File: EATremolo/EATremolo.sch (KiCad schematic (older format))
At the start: 37 parts, among them J1 JACK__MONO_2P_NC, J2 BARREL_JACK, J3 JACK__MONO_2P_NC, Q1 Q_NJFET_DSG, Q2 Q_NPN_EBC, Q3 Q_NPN_EBC, Q4 Q_NJFET_DSG, SW1 SW_3PDT_on_on

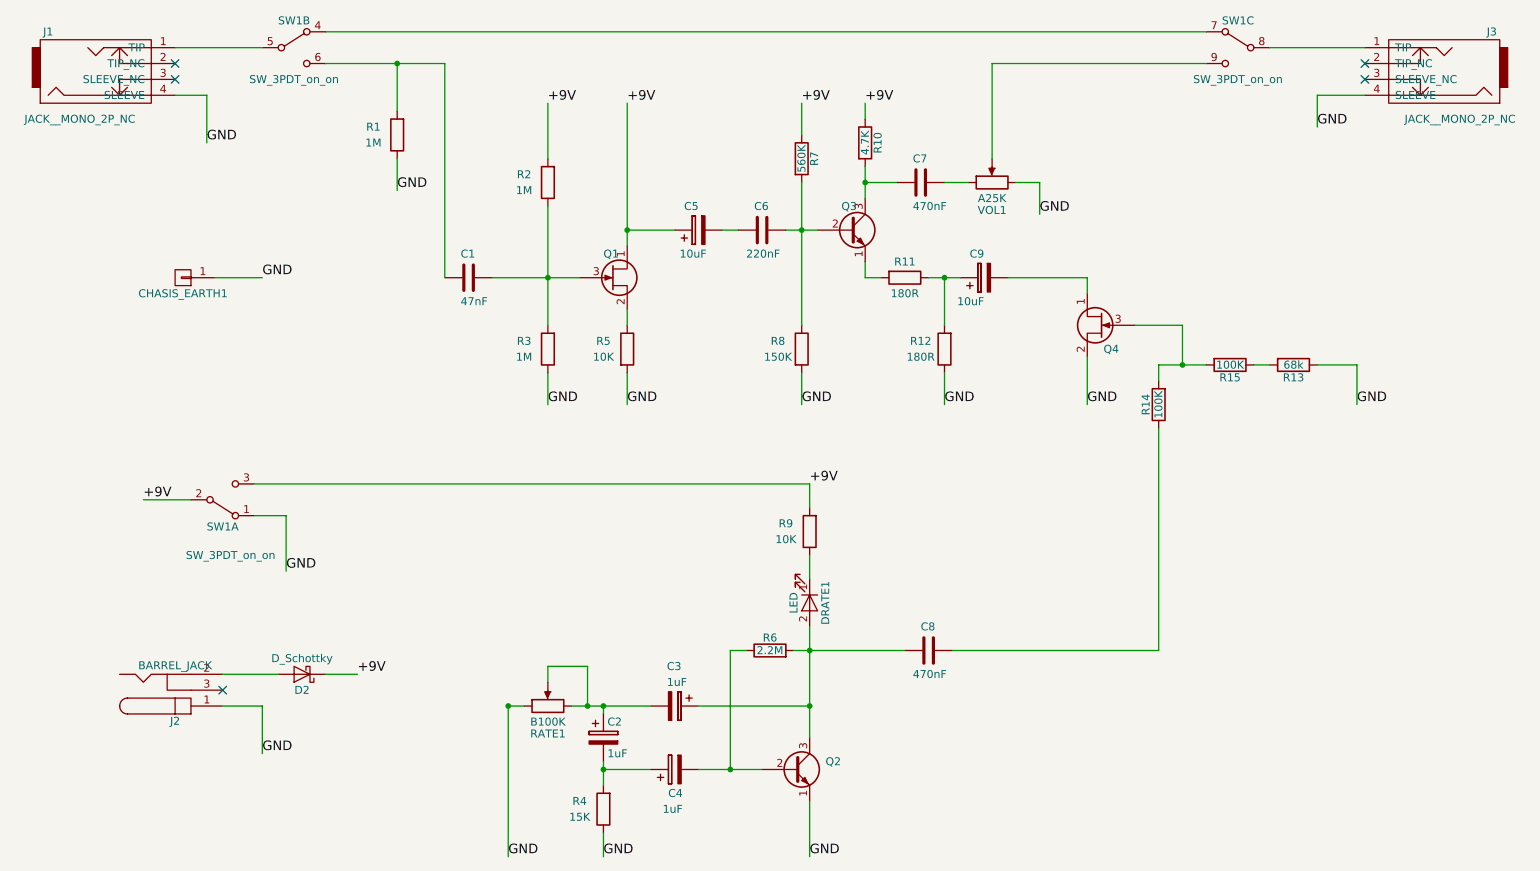
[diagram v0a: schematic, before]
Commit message: EA Tremolo Layout completed
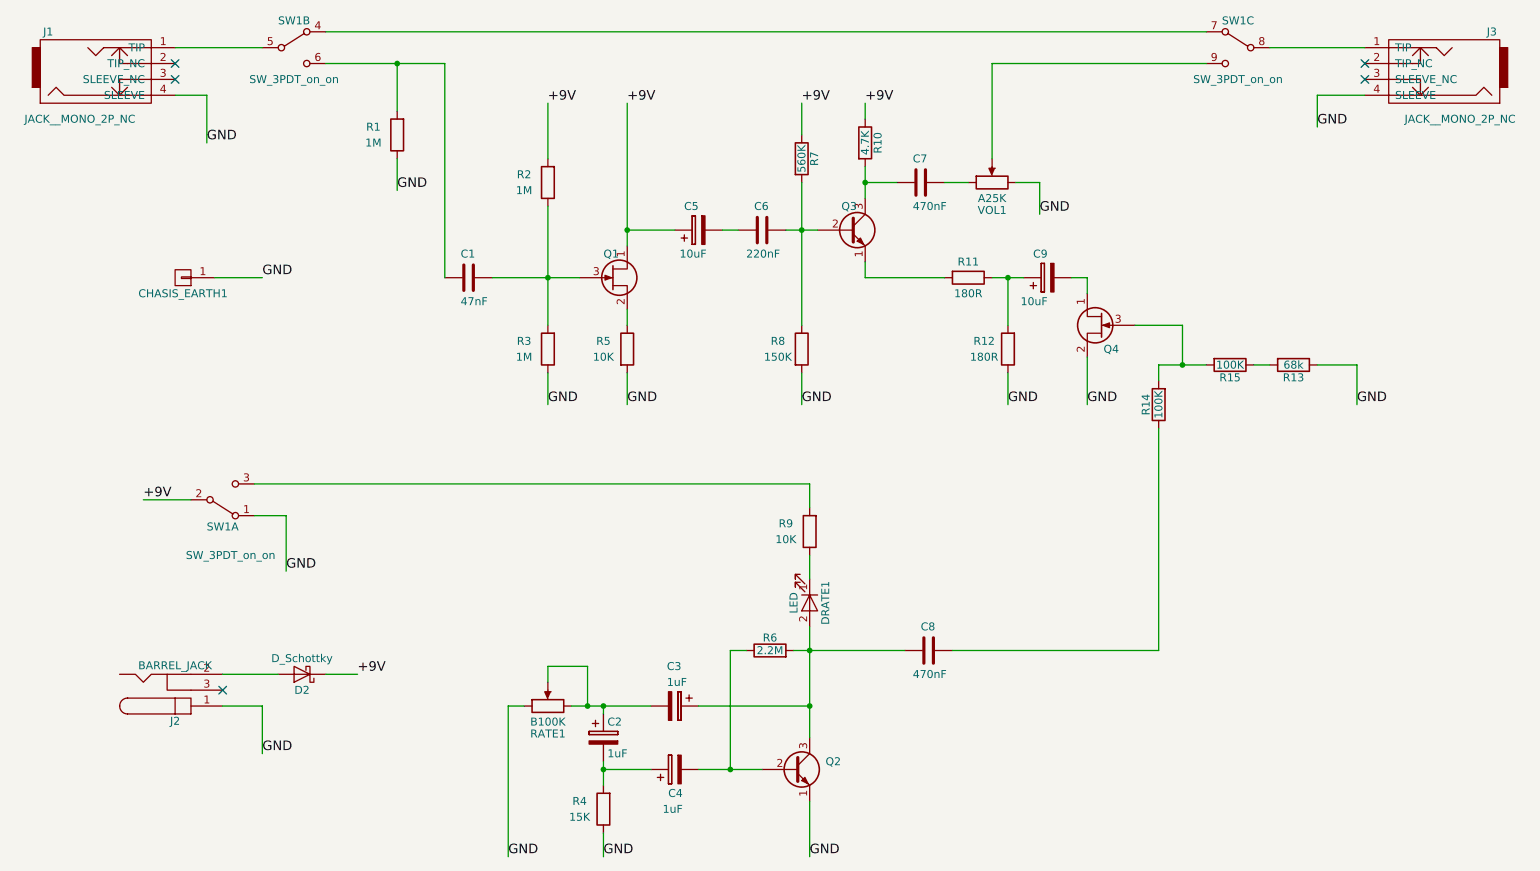
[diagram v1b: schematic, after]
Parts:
- D2: footprint Diodes_THT:D_DO-41_SOD81_P10.16mm_Horizontal -> Diodes_THT:D_DO-41_SOD81_P2.54mm_Vertical_AnodeUp
- R1, R10, R12, R13, R14, R15, R2, R3, R4, R5, R6, R7, R8, R9: footprint R_Axial_DIN0207_L6.3mm_D2.5mm_P7:R_Axial_DIN0207_L6.3mm_D2.5mm_P7.62mm_Horizontal_PS2_DH1 -> R_Axial_DIN0207_Vertical_2mmPad:R_Axial_DIN0207_Vertical_2mmPad
- R11: footprint R_Axial_DIN0207_L6.3mm_D2.5mm_P7:R_Axial_DIN0207_L6.3mm_D2.5mm_P7.62mm_Horizontal_PS2_DH1 -> Resistors_THT:R_Axial_DIN0207_L6.3mm_D2.5mm_P5.08mm_Vertical
- RATE1, VOL1: footprint TEConnPotentiometer:TEConnPot_23mm_20mm -> Potentiometers:Potentiometer_Omeg_PC16PU_Horizontal
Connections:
- net +9V: no longer R9.2, SW1.3 (C)
- new net: R9.2, SW1.3 (C)
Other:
- moved on the sheet: C9, R11, R12

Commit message: saved EATremolo
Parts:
- C5: footprint CP_Radial_D4_P2_PadSize2_Drill1:CP_Radial_D4_P2_PadSize2_Drill1 -> C_Disc_P5:C_Disc_P5.0mm_2mmPads
- C7: footprint C_Disc_2mmPads:C_Disc_2mmPads -> C_Disc_P5:C_Disc_P5.0mm_2mmPads
- R5: footprint R_Axial_DIN0207_Vertical_2mmPad:R_Axial_DIN0207_Vertical_2mmPad -> R_Axial_DIN0207_P5:R_Axial_DIN0207_P5.08mm_2mmPads
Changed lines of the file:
@@
 F 0 "R5" H 4550 3500 50  0000 C CNN
 F 1 "10K" H 4550 3400 50  0000 C CNN
-F 2 "R_Axial_DIN0207_Vertical_2mmPad:R_Axial_DIN0207_Vertical_2mmPad" V 4630 3450 50  0001 C CNN
+F 2 "R_Axial_DIN0207_P5:R_Axial_DIN0207_P5.08mm_2mmPads" V 4630 3450 50  0001 C CNN
 F 3 "" H 4700 3450 50  0001 C CNN
 	1    4700 3450
@@
 F 0 "C5" V 5300 2700 50  0000 L CNN
 F 1 "10uF" V 5000 2650 50  0000 L CNN
-F 2 "CP_Radial_D4_P2_PadSize2_Drill1:CP_Radial_D4_P2_PadSize2_Drill1" H 5188 2550 50  0001 C CNN
+F 2 "C_Disc_P5:C_Disc_P5.0mm_2mmPads" H 5188 2550 50  0001 C CNN
 F 3 "" H 5150 2700 50  0001 C CNN
 	1    5150 2700
@@
 F 0 "C7" V 6400 2350 50  0000 L CNN
 F 1 "470nF" V 6700 2350 50  0000 L CNN
-F 2 "C_Disc_2mmPads:C_Disc_2mmPads" H 6588 2250 50  0001 C CNN
+F 2 "C_Disc_P5:C_Disc_P5.0mm_2mmPads" H 6588 2250 50  0001 C CNN
 F 3 "" H 6550 2400 50  0001 C CNN
 	1    6550 2400
@@
 	2400 5700 2400 6000
 Wire Wire Line
-	2800 1650 3250 1650
-Wire Wire Line
-	3250 1650 3550 1650
+	2800 1650 3550 1650
 Wire Wire Line
 	3250 1650 3250 1950
@@
 	3250 2250 3250 2450
 Wire Wire Line
-	4200 2550 4200 3000
-Wire Wire Line
-	4200 3000 4200 3300
+	4200 2550 4200 3300
 Wire Wire Line
 	4200 3600 4200 3800
 Connection ~ 3250 1650
 Wire Wire Line
-	3850 3000 4200 3000
-Wire Wire Line
-	4200 3000 4400 3000
+	3850 3000 4400 3000
 Connection ~ 4200 3000
 Wire Wire Line
@@
 	4700 3600 4700 3800
 Wire Wire Line
-	4700 1900 4700 2700
-Wire Wire Line
-	4700 2700 4700 2800
+	4700 1900 4700 2800
 Wire Wire Line
 	5000 2700 4700 2700
@@
 	5800 2100 5800 1900
 Wire Wire Line
-	6200 2300 6200 2400
-Wire Wire Line
-	6200 2400 6200 2500
+	6200 2300 6200 2500
 Connection ~ 5800 2700
 Wire Wire Line
-	5800 2400 5800 2700
-Wire Wire Line
-	5800 2700 5800 3300
-Wire Wire Line
-	5700 2700 5800 2700
-Wire Wire Line
-	5800 2700 5900 2700
+	5800 2400 5800 3300
+Wire Wire Line
+	5700 2700 5900 2700
 Wire Wire Line
 	6200 2900 6200 3000
@@
 	7100 3300 7100 3000
 Wire Wire Line
-	7000 3000 7100 3000
-Wire Wire Line
-	7100 3000 7200 3000
+	7000 3000 7200 3000
 Wire Wire Line
 	7100 3600 7100 3800
@@
 	8050 5350 6750 5350
 Wire Wire Line
-	5850 5200 5850 5350
-Wire Wire Line
-	5850 5350 5850 5700
-Wire Wire Line
-	5850 5700 5850 5900
+	5850 5200 5850 5900
 Connection ~ 5850 5350
 Wire Wire Line
@@
 	5850 6300 5850 6650
 Wire Wire Line
-	5750 5350 5850 5350
-Wire Wire Line
-	5850 5350 6450 5350
+	5750 5350 6450 5350
 Wire Wire Line
 	5150 5700 5850 5700
 Connection ~ 5850 5700
 Wire Wire Line
-	4350 5700 4450 5700
-Wire Wire Line
-	4450 5700 4550 5700
-Wire Wire Line
-	4550 5700 4850 5700
+	4350 5700 4850 5700
 Wire Wire Line
 	4550 5700 4550 5750
 Wire Wire Line
-	4550 6050 4550 6100
-Wire Wire Line
-	4550 6100 4550 6200
+	4550 6050 4550 6200
 Wire Wire Line
 	4550 6100 4850 6100
@@
 	5350 5350 5350 6100
 Wire Wire Line
-	5150 6100 5350 6100
-Wire Wire Line
-	5350 6100 5550 6100
+	5150 6100 5550 6100
 Connection ~ 5350 6100
 Connection ~ 4550 6100
@@
 	8750 3550 8650 3550
 Wire Wire Line
-	8050 3550 8200 3550
-Wire Wire Line
-	8200 3550 8350 3550
+	8050 3550 8350 3550
 Wire Wire Line
 	8050 3550 8050 3650

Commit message: EA Tremolo Rev2
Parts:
- added R16: 1K, R_Axial_DIN0207_Vertical_2mmPad:R_Axial_DIN0207_Vertical_2mmPad, symbol R
- C2, C3, C4: footprint CP_Radial_D4_P2_PadSize2_Drill1:CP_Radial_D4_P2_PadSize2_Drill1 -> C_Disc_2mmPads:C_Disc_2mmPads
- R11: footprint Resistors_THT:R_Axial_DIN0207_L6.3mm_D2.5mm_P5.08mm_Vertical -> R_Axial_DIN0207_P5:R_Axial_DIN0207_P5.08mm_2mmPads
- R12: value 180R -> 1.2K
- R14: value 100K -> 180K
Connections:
- net +9V: no longer C5.1
- net GND: no longer SW1.1 (A)
- net at C3.1, C8.2, Q2.3 (C)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: now also DRATE1.1 (K); no longer DRATE1.2 (A)
- net at Q1.2 (S), R5.1: now also C5.1
- net at R9.1: now also DRATE1.2 (A); no longer DRATE1.1 (K)
- net at C2.1, C3.2: now also R16.1; no longer RATE1.2, RATE1.3
- new net: R16.2, RATE1.2, RATE1.3
- no-connect marks 5 -> 6
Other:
- moved on the sheet: DRATE1, RATE1
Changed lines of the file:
@@
 F 0 "R11" V 6750 3000 50  0000 C CNN
 F 1 "180R" V 6950 3000 50  0000 C CNN
-F 2 "Resistors_THT:R_Axial_DIN0207_L6.3mm_D2.5mm_P5.08mm_Vertical" V 6780 3000 50  0001 C CNN
+F 2 "R_Axial_DIN0207_P5:R_Axial_DIN0207_P5.08mm_2mmPads" V 6780 3000 50  0001 C CNN
 F 3 "" H 6850 3000 50  0001 C CNN
 	1    6850 3000
@@
 P 7100 3450
 F 0 "R12" H 7250 3400 50  0000 C CNN
-F 1 "180R" H 7250 3500 50  0000 C CNN
+F 1 "1.2K" H 7250 3500 50  0000 C CNN
 F 2 "R_Axial_DIN0207_Vertical_2mmPad:R_Axial_DIN0207_Vertical_2mmPad" V 7030 3450 50  0001 C CNN
 F 3 "" H 7100 3450 50  0001 C CNN
@@
 F 0 "C3" V 4750 5650 50  0000 L CNN
 F 1 "1uF" V 4850 5650 50  0000 L CNN
-F 2 "CP_Radial_D4_P2_PadSize2_Drill1:CP_Radial_D4_P2_PadSize2_Drill1" H 5038 5550 50  0001 C CNN
+F 2 "C_Disc_2mmPads:C_Disc_2mmPads" H 5038 5550 50  0001 C CNN
 F 3 "" H 5000 5700 50  0001 C CNN
 	1    5000 5700
@@
 F 0 "C4" V 4850 6050 50  0000 L CNN
 F 1 "1uF" V 4750 6050 50  0000 L CNN
-F 2 "CP_Radial_D4_P2_PadSize2_Drill1:CP_Radial_D4_P2_PadSize2_Drill1" H 5038 5950 50  0001 C CNN
+F 2 "C_Disc_2mmPads:C_Disc_2mmPads" H 5038 5950 50  0001 C CNN
 F 3 "" H 5000 6100 50  0001 C CNN
 	1    5000 6100
@@
 F 0 "C2" H 4575 6000 50  0000 L CNN
 F 1 "1uF" H 4575 5800 50  0000 L CNN
-F 2 "CP_Radial_D4_P2_PadSize2_Drill1:CP_Radial_D4_P2_PadSize2_Drill1" H 4588 5750 50  0001 C CNN
+F 2 "C_Disc_2mmPads:C_Disc_2mmPads" H 4588 5750 50  0001 C CNN
 F 3 "" H 4550 5900 50  0001 C CNN
 	1    4550 5900
@@
 L POT RATE1
 U 1 1 5A224067
-P 4200 5700
-F 0 "RATE1" V 4025 5700 50  0000 C CNN
-F 1 "B100K" V 4100 5700 50  0000 C CNN
-F 2 "Potentiometers:Potentiometer_Omeg_PC16PU_Horizontal" H 4200 5700 50  0001 C CNN
-F 3 "" H 4200 5700 50  0001 C CNN
-	1    4200 5700
-	0    -1   -1   0
-$EndComp
-Text Label 3950 6650 0    60   ~ 0
+P 3750 5700
+F 0 "RATE1" V 3575 5700 50  0000 C CNN
+F 1 "B100K" V 3650 5700 50  0000 C CNN
+F 2 "Potentiometers:Potentiometer_Omeg_PC16PU_Horizontal" H 3750 5700 50  0001 C CNN
+F 3 "" H 3750 5700 50  0001 C CNN
+	1    3750 5700
+	0    -1   -1   0
+$EndComp
+Text Label 3500 6650 0    60   ~ 0
 GND
 $Comp
@@
 F 3 "" H 5850 5050 50  0001 C CNN
 	1    5850 5050
-	0    1    1    0
-$EndComp
-Text Label 2550 4850 0    60   ~ 0
-GND
+	0    -1   -1   0
+$EndComp
 NoConn ~ 2150 5600
 $Comp
@@
 P 8050 3800
 F 0 "R14" V 8130 3800 50  0000 C CNN
-F 1 "100K" V 8050 3800 50  0000 C CNN
+F 1 "180K" V 8050 3800 50  0000 C CNN
 F 2 "R_Axial_DIN0207_Vertical_2mmPad:R_Axial_DIN0207_Vertical_2mmPad" V 7980 3800 50  0001 C CNN
 F 3 "" H 8050 3800 50  0001 C CNN
@@
 	4700 1900 4700 2800
 Wire Wire Line
-	5000 2700 4700 2700
-Connection ~ 4700 2700
-Wire Wire Line
 	5300 2700 5400 2700
 Wire Wire Line
@@
 Connection ~ 5850 5700
 Wire Wire Line
-	4350 5700 4850 5700
+	3900 5700 4100 5700
+Wire Wire Line
+	4400 5700 4850 5700
 Wire Wire Line
 	4550 5700 4550 5750
@@
 Connection ~ 4550 5700
 Wire Wire Line
-	4050 5700 3950 5700
+	3600 5700 3500 5700
 Wire Wire Line
 	2050 1850 2050 2150
@@
 Wire Wire Line
 	1950 4400 1650 4400
-Wire Wire Line
-	2350 4500 2550 4500
-Wire Wire Line
-	2550 4500 2550 4850
 Wire Wire Line
 	5850 4300 2350 4300
@@
 Connection ~ 8200 3550
 Wire Wire Line
-	3950 5700 3950 6650
-Wire Wire Line
-	4200 5550 4200 5450
-Wire Wire Line
-	4200 5450 4450 5450
-Wire Wire Line
-	4450 5450 4450 5700
-Connection ~ 4450 5700
+	3500 5700 3500 6650
+Wire Wire Line
+	3750 5550 3750 5450
+Wire Wire Line
+	3750 5450 3950 5450
+Wire Wire Line
+	3950 5450 3950 5700
+Connection ~ 3950 5700
 Wire Wire Line
 	2100 3000 2400 3000
+$Comp
+L R R16
+U 1 1 5A23D88A
+P 4250 5700
+F 0 "R16" V 4330 5700 50  0000 C CNN
+F 1 "1K" V 4250 5700 50  0000 C CNN
+F 2 "R_Axial_DIN0207_Vertical_2mmPad:R_Axial_DIN0207_Vertical_2mmPad" V 4180 5700 50  0001 C CNN
+F 3 "" H 4250 5700 50  0001 C CNN
+	1    4250 5700
+	0    1    1    0
+$EndComp
+Wire Wire Line
+	4700 3250 4900 3250
+Wire Wire Line
+	4900 3250 4900 2700
+Connection ~ 4700 3250
+Wire Wire Line
+	4900 2700 5000 2700
+NoConn ~ 2350 4500
 $EndSCHEMATC
